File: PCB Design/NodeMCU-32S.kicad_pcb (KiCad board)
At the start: 2 copper layers, 85.4 x 61.5 mm, 19 parts, among them J1 Screw_Terminal_01x02, J2 Screw_Terminal_01x02, J3 Screw_Terminal_01x02, J4 Screw_Terminal_01x02, J5 Screw_Terminal_01x03, Q1 IRFZ44N, SW1 SW_DPDT_x2, U1 ESP32-DevKitC, U2 Generic_5v_Module

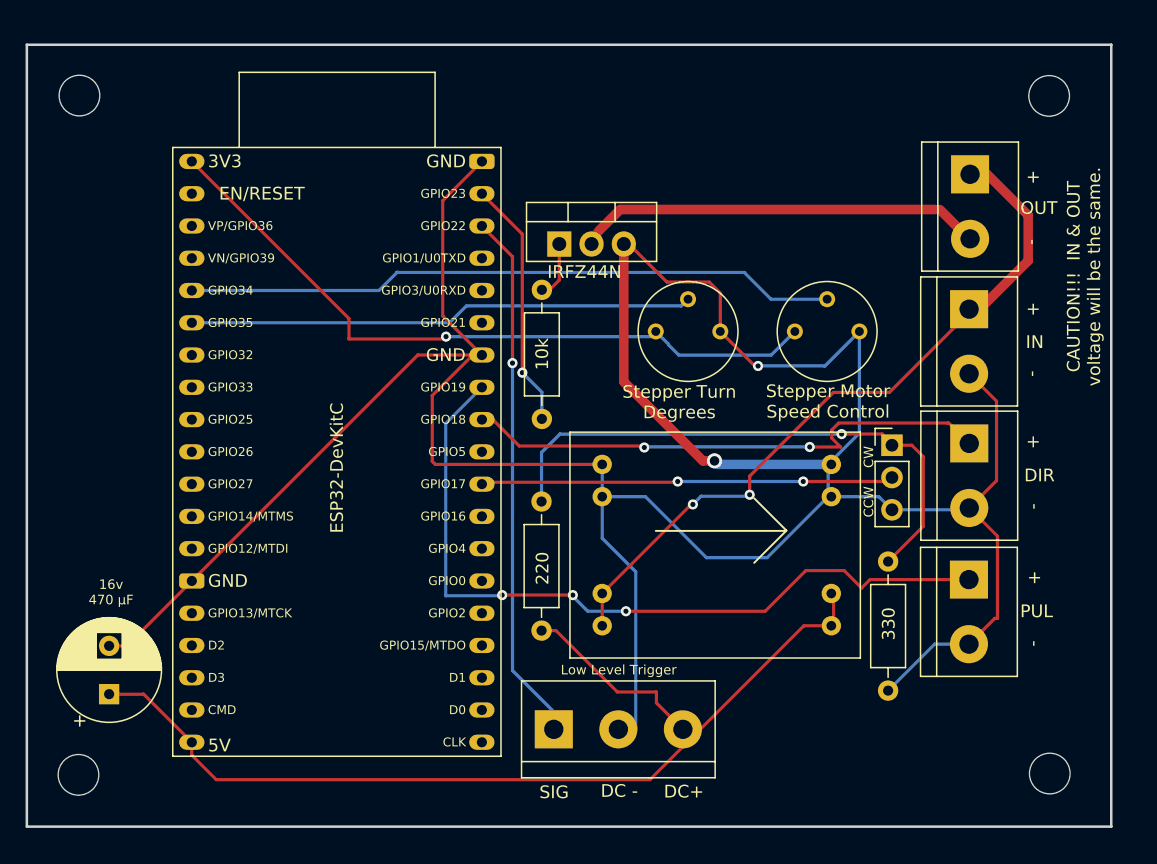
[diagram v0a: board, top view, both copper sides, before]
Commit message: PCB changes
Pluggable Stepper Motor
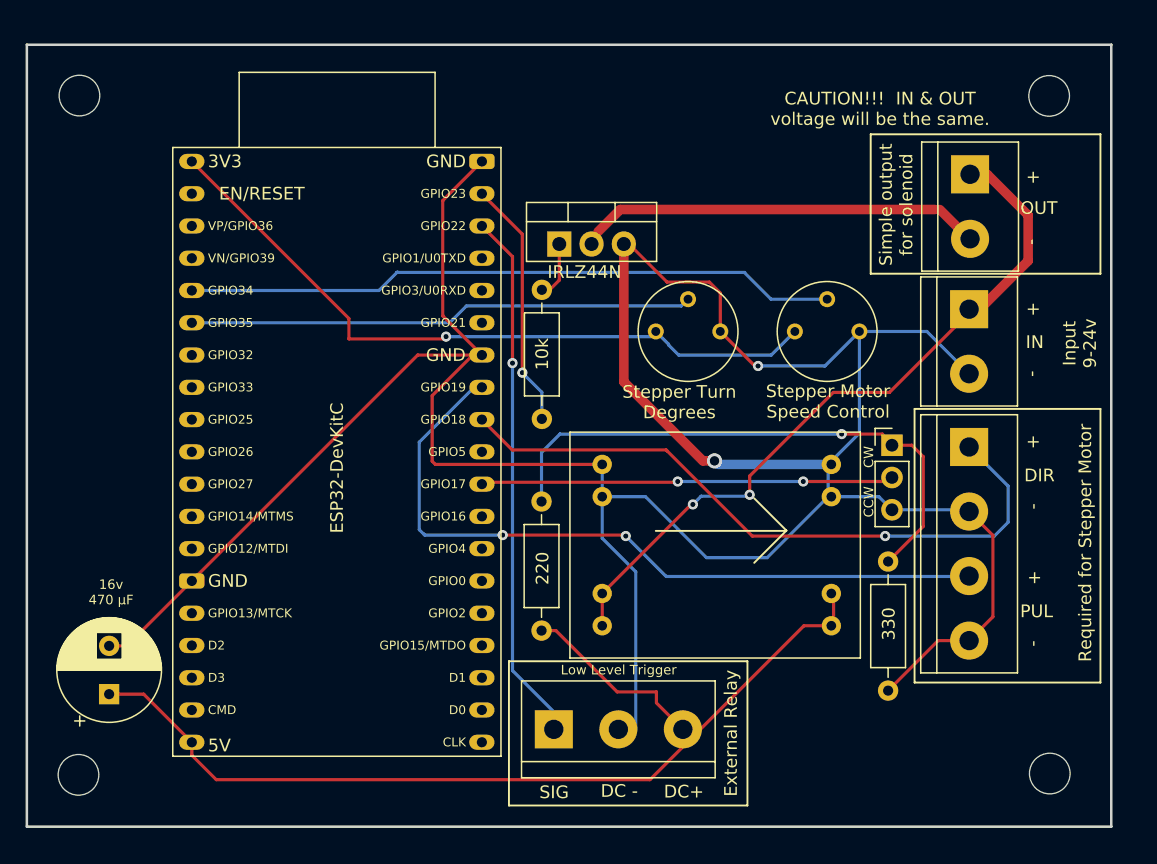
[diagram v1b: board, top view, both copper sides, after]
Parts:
- removed J4: Screw_Terminal_01x02, TerminalBlock:TerminalBlock_bornier-2_P5.08mm
- J3: value Screw_Terminal_01x02 -> Screw_Terminal_01x04; footprint TerminalBlock:TerminalBlock_bornier-2_P5.08mm -> TerminalBlock:TerminalBlock_bornier-4_P5.08mm
- Q1: value IRFZ44N -> IRLZ44N
- moved J3 0.28 mm to (133.6, 83.4)
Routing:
- net DIR: track 42.4 -> 52.9 mm, vias 2 -> 1
- net GND: track 237.5 -> 234.3 mm
- net PUL: track 61.5 -> 58.4 mm, vias 3 -> 2
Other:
- board text added: "External Relay"
- board text added: "Input 9-24v"
- board text added: "Required for Stepper Motor"
- board text added: "Simple output for solenoid"

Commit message: Cleanerer
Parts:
- moved SW1 24.9 mm to (141.0, 104.3), turned to -90 degrees
- moved R4 4.72 mm to (127.2, 87.7)
- moved H1 0.93 mm to (139.6, 110.0)
- moved H3 0.89 mm to (63.6, 110.1)
- moved H4 0.81 mm to (139.9, 55.0)
- moved H2 0.81 mm to (63.6, 55.0)
- moved J2 0.08 mm to (133.7, 72.6)
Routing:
- net Net-(SW1-Pad2): track 32.6 -> 52.3 mm, vias 2 -> 4
- net Net-(R3-Pad2): track 44.7 -> 60.8 mm
- net GND: track 234.3 -> 247.9 mm
- net MOSFET_GND: track 31.5 -> 35.6 mm
- net VCC: track 56.7 -> 60.1 mm
- net +5V: track 82.7 -> 80.5 mm
- net lowActivationPin: track 42.5 -> 44.2 mm
- net Net-(Q1-Pad1): track 3.96 -> 3.25 mm
- net PUL: track 58.4 -> 57.8 mm
- net +3V3: track 56.0 -> 56.6 mm
- net SPEED_POT: track 51.5 -> 51.0 mm
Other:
- board size 85.4 x 61.5 mm -> 85.4 x 63.7 mm
- board text added: "Board Design 1.7"
- board text added: "Solenoid Out Vout = Vin when Activated"
- board text removed: "Board Design 1.6"
- board text removed: "CAUTION!!! IN & OUT voltage will be the same."
- board text removed: "Simple output for solenoid"

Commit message: Update NodeMCU-32S.kicad_pcb
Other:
- board size 85.4 x 63.7 mm -> 86.9 x 63.7 mm
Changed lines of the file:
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@@
       (effects (font (size 1 1) (thickness 0.15)))
     )
-    (fp_text value "Screw_Terminal_01x02" (at 2.54 5.08 90) (layer "F.Fab")
+    (fp_text value "Screw_Terminal_01x02" (at 2.54 5.08 90) (layer "F.Fab") hide
       (effects (font (size 1 1) (thickness 0.15)))
     )
@@
       (effects (font (size 1 1) (thickness 0.15)))
     )
-    (fp_text value "R_Potentiometer_Trim_US" (at 0 2.52 -90) (layer "F.Fab")
+    (fp_text value "R_Potentiometer_Trim_US" (at 0 2.52 -90) (layer "F.Fab") hide
       (effects (font (size 1 1) (thickness 0.15)))
     )
@@
       (effects (font (size 1 1) (thickness 0.15)))
     )
-    (fp_text value "Screw_Terminal_01x02" (at 13.4112 5.1181 90) (layer "F.Fab")
+    (fp_text value "Screw_Terminal_01x02" (at 13.4112 5.1181 90) (layer "F.Fab") hide
       (effects (font (size 1 1) (thickness 0.15)))
     )
@@
   (gr_line (start 119.2022 90.0176) (end 116.6622 92.5576) (layer "F.SilkS") (width 0.15))
   (gr_rect (start 129.6162 59.1566) (end 143.9164 69.7992) (layer "F.SilkS") (width 0.15) (fill none))
-  (gr_rect (start 59.4106 50.3555) (end 144.7682 114.0333) (layer "Edge.Cuts") (width 0.2) (fill none))
+  (gr_rect (start 59.397 50.4825) (end 146.304 114.1603) (layer "Edge.Cuts") (width 0.2) (fill none))
   (gr_text "Board Design 1.7\n\n\n" (at 83.82 55.88) (layer "B.SilkS")
     (effects (font (size 2 2) (thickness 0.25)) (justify mirror))

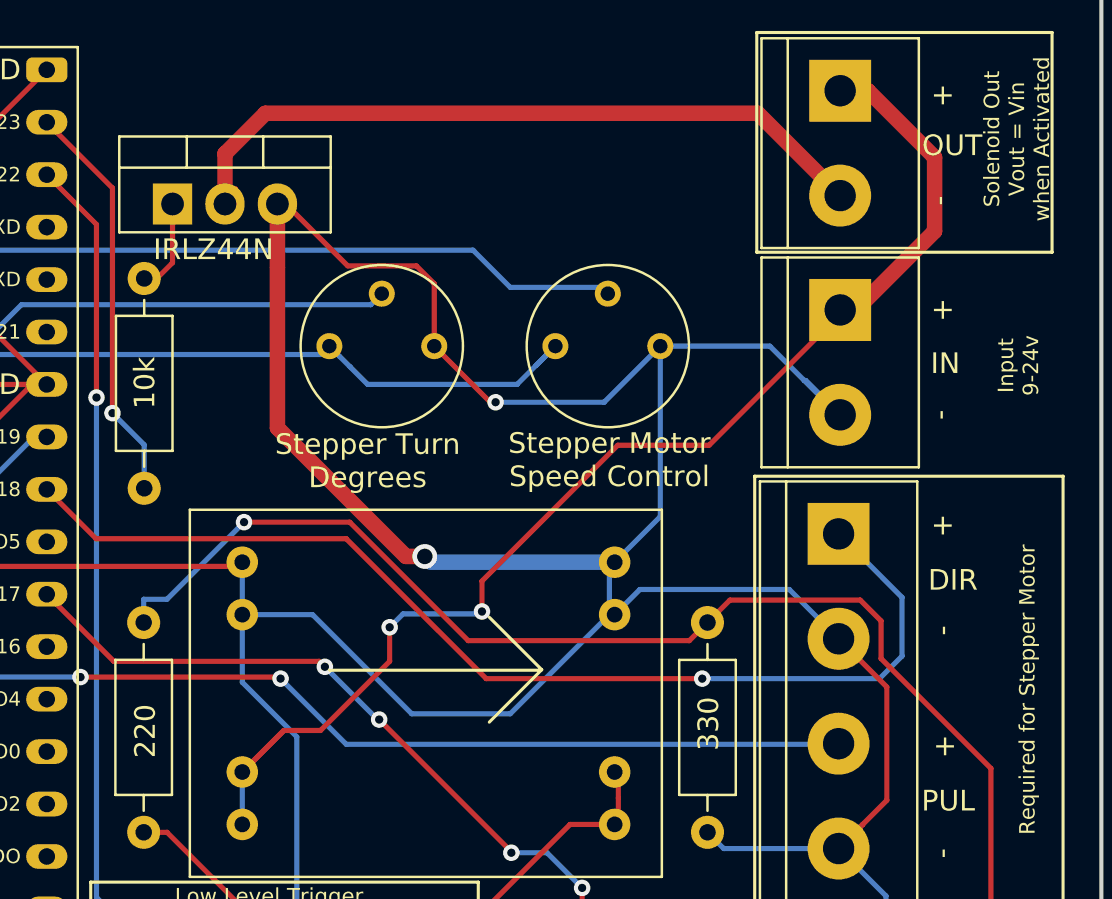
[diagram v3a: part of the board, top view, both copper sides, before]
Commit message: photos, cleaned up PCB design
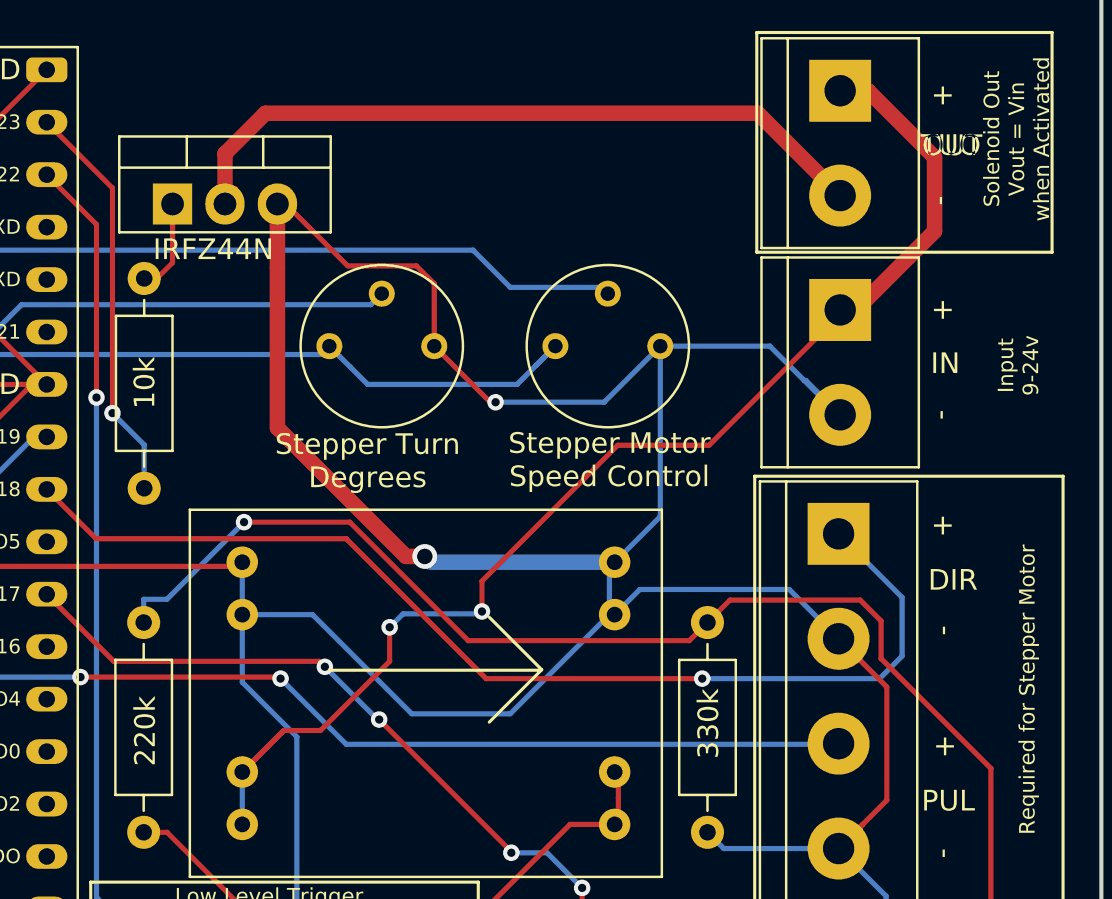
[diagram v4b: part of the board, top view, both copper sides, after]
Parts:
- Q1: value IRLZ44N -> IRFZ44N
- R3: value 220 -> 220k
- R4: value 330 -> 330k
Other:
- board text added: "Board Design 1.8"
- board text removed: "Board Design 1.7"
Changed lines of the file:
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@@
       (effects (font (size 1 1) (thickness 0.15)))
     )
-    (fp_text value "IRLZ44N" (at 1.9812 2.2046) (layer "F.SilkS")
+    (fp_text value "IRFZ44N" (at 1.9812 2.2046) (layer "F.SilkS")
       (effects (font (size 1 1) (thickness 0.15)))
     )
@@
       (effects (font (size 1 1) (thickness 0.15)))
     )
-    (fp_text value "330" (at 4.9022 -0.0508 90) (layer "F.SilkS")
+    (fp_text value "330k" (at 4.9022 -0.0508 90) (layer "F.SilkS")
       (effects (font (size 1 1) (thickness 0.15)))
     )
@@
       (effects (font (size 1 1) (thickness 0.15)))
     )
-    (fp_text value "220" (at 4.9022 0.0762 90) (layer "F.SilkS")
+    (fp_text value "220k" (at 4.9022 0.0762 90) (layer "F.SilkS")
       (effects (font (size 1 1) (thickness 0.15)))
     )
@@
   (gr_rect (start 129.6162 59.1566) (end 143.9164 69.7992) (layer "F.SilkS") (width 0.15) (fill none))
   (gr_rect (start 59.397 50.4825) (end 146.304 114.1603) (layer "Edge.Cuts") (width 0.2) (fill none))
-  (gr_text "Board Design 1.7\n\n\n" (at 83.82 55.88) (layer "B.SilkS")
+  (gr_text "Low Level Trigger" (at 106.3752 108.7628) (layer "B.SilkS")
+    (effects (font (size 0.75 0.75) (thickness 0.125)) (justify mirror))
+  )
+  (gr_text "-" (at 138.6078 98.8822 90) (layer "B.SilkS")
+    (effects (font (size 1 1) (thickness 0.15)))
+  )
+  (gr_text "Board Design 1.8\n\n\n" (at 83.82 55.88) (layer "B.SilkS")
     (effects (font (size 2 2) (thickness 0.25)) (justify mirror))
+  )
+  (gr_text "-" (at 138.6586 67.2846 -90) (layer "B.SilkS")
+    (effects (font (size 1 1) (thickness 0.15)) (justify mirror))
+  )
+  (gr_text "Solenoid Out\nVout = Vin\nwhen Activated" (at 142.1892 64.4652 90) (layer "B.SilkS")
+    (effects (font (size 0.75 0.75) (thickness 0.15)) (justify mirror))
+  )
+  (gr_text "PUL\n" (at 139.0396 96.3676) (layer "B.SilkS")
+    (effects (font (size 1 1) (thickness 0.15)) (justify mirror))
+  )
+  (gr_text "+" (at 138.8364 72.5932 -90) (layer "B.SilkS")
+    (effects (font (size 1 1) (thickness 0.15)))
+  )
+  (gr_text "IN" (at 138.7348 75.2094) (layer "B.SilkS")
+    (effects (font (size 1 1) (thickness 0.15)) (justify mirror))
+  )
+  (gr_text "DIR" (at 139.0904 85.6742) (layer "B.SilkS")
+    (effects (font (size 1 1) (thickness 0.15)) (justify mirror))
+  )
+  (gr_text "+" (at 138.7094 93.7514 90) (layer "B.SilkS")
+    (effects (font (size 1 1) (thickness 0.15)))
+  )
+  (gr_text "Required for Stepper Motor" (at 142.6718 91.2114 90) (layer "B.SilkS")
+    (effects (font (size 0.75 0.75) (thickness 0.15)) (justify mirror))
+  )
+  (gr_text "+" (at 138.5824 82.9818 90) (layer "B.SilkS")
+    (effects (font (size 1 1) (thickness 0.15)))
+  )
+  (gr_text "SIG" (at 101.0666 110.6678) (layer "B.SilkS")
+    (effects (font (size 1 1) (thickness 0.15)) (justify mirror))
+  )
+  (gr_text "DC -\n" (at 105.8672 110.5154) (layer "B.SilkS")
+    (effects (font (size 1 1) (thickness 0.15)) (justify mirror))
+  )
+  (gr_text "DC+\n" (at 110.7694 110.617) (layer "B.SilkS")
+    (effects (font (size 1 1) (thickness 0.15)) (justify mirror))
+  )
+  (gr_text "-" (at 138.7348 77.597 -90) (layer "B.SilkS")
+    (effects (font (size 1 1) (thickness 0.15)))
+  )
+  (gr_text "-" (at 138.6332 88.138 90) (layer "B.SilkS")
+    (effects (font (size 1 1) (thickness 0.15)))
+  )
+  (gr_text "+" (at 138.811 62.1792 -90) (layer "B.SilkS")
+    (effects (font (size 1 1) (thickness 0.15)))
+  )
+  (gr_text "Input\n9-24v" (at 142.3162 75.2094 90) (layer "B.SilkS")
+    (effects (font (size 0.75 0.75) (thickness 0.15)) (justify mirror))
   )
   (gr_text "DIR" (at 139.1158 85.678049) (layer "F.SilkS")
@@
     (effects (font (size 1 1) (thickness 0.15)))
   )
+  (gr_text "OUT" (at 139.0142 64.6176) (layer "F.SilkS")
+    (effects (font (size 1 1) (thickness 0.15)) (justify mirror))
+  )
   (gr_text "-" (at 138.6586 77.6732 -90) (layer "F.SilkS")
